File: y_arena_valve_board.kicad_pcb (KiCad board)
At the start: 2 copper layers, 0 parts

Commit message: Initial pcb import
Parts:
- added D1: diode_low_rev_current, y_arena_valve_board:SOD-123, F.Cu at (181.2, 52.2)
- added D10: LED_GRN, y_arena_valve_board:LED0805, F.Cu at (245.0, 25.8)
- added D11: diode_low_rev_current, y_arena_valve_board:SOD-123, F.Cu at (209.4, 52.2)
- added D12: LED_GRN, y_arena_valve_board:LED0805, F.Cu at (213.2, 52.9)
- added D13: diode_low_rev_current, y_arena_valve_board:SOD-123, F.Cu at (227.1, 43.6)
- added D14: LED_GRN, y_arena_valve_board:LED0805, F.Cu at (230.9, 44.2)
- added D15: diode_low_rev_current, y_arena_valve_board:SOD-123, F.Cu at (241.1, 34.4)
- added D16: LED_GRN, y_arena_valve_board:LED0805, F.Cu at (245.0, 35.0)
- added D17: diode_low_rev_current, y_arena_valve_board:SOD-123, F.Cu at (223.5, 52.8)
- added D18: LED_GRN, y_arena_valve_board:LED0805, F.Cu at (227.3, 53.5)
- added D2: LED_GRN, y_arena_valve_board:LED0805, F.Cu at (185.1, 52.9)
- added D3: diode_low_rev_current, y_arena_valve_board:SOD-123, F.Cu at (227.1, 25.1)
- added D4: LED_GRN, y_arena_valve_board:LED0805, F.Cu at (230.9, 25.8)
- added D5: diode_low_rev_current, y_arena_valve_board:SOD-123, F.Cu at (195.3, 52.2)
- added D6: LED_GRN, y_arena_valve_board:LED0805, F.Cu at (199.1, 52.9)
- added D7: diode_low_rev_current, y_arena_valve_board:SOD-123, F.Cu at (227.1, 34.4)
- added D8: LED_GRN, y_arena_valve_board:LED0805, F.Cu at (230.9, 35.0)
- added D9: diode_low_rev_current, y_arena_valve_board:SOD-123, F.Cu at (241.1, 25.1)
- added FID1: FIDUCIAL, y_arena_valve_board:FIDUCIAL, F.Cu at (219.3, 24.9)
- added FID2: FIDUCIAL, y_arena_valve_board:FIDUCIAL, F.Cu at (188.9, 43.5)
- added FID3: FIDUCIAL, y_arena_valve_board:FIDUCIAL, F.Cu at (186.3, 43.5)
- added FID4: FIDUCIAL, y_arena_valve_board:FIDUCIAL, F.Cu at (205.2, 37.2)
- added MH1: MOUNTING_HOLE_4-40, y_arena_valve_board:MOUNTING_HOLE_4-40, F.Cu at (92.1, 101.0)
- added MH2: MOUNTING_HOLE_4-40, y_arena_valve_board:MOUNTING_HOLE_4-40, F.Cu at (120.0, 72.4)
- added MH3: MOUNTING_HOLE_4-40, y_arena_valve_board:MOUNTING_HOLE_4-40, F.Cu at (64.1, 72.4)
- added P1: HEADER_02X12_SMD, y_arena_valve_board:HEADER_02x12_SMD, F.Cu at (213.4, 62.2)
- added R1: 499, y_arena_valve_board:SM0805, F.Cu at (187.7, 52.8)
- added R2: 499, y_arena_valve_board:SM0805, F.Cu at (233.6, 25.7)
- added R3: 499, y_arena_valve_board:SM0805, F.Cu at (201.8, 52.8)
- added R4: 499, y_arena_valve_board:SM0805, F.Cu at (233.6, 35.0)
- added R5: 499, y_arena_valve_board:SM0805, F.Cu at (247.6, 25.7)
- added R6: 499, y_arena_valve_board:SM0805, F.Cu at (215.9, 52.8)
- added R7: 499, y_arena_valve_board:SM0805, F.Cu at (233.6, 44.2)
- added R8: 499, y_arena_valve_board:SM0805, F.Cu at (247.6, 35.0)
- added R9: 499, y_arena_valve_board:SM0805, F.Cu at (230.0, 53.4)
- added S1: LEECO_LHDB, y_arena_valve_board:LEECO_LHDB, B.Cu at (129.5, 33.0)
- added S2: LEECO_LHDB, y_arena_valve_board:LEECO_LHDB, B.Cu at (80.6, 22.2)
- added S3: LEECO_LHDB, y_arena_valve_board:LEECO_LHDB, B.Cu at (80.6, 34.9)
- added S4: LEECO_LHDB, y_arena_valve_board:LEECO_LHDB, B.Cu at (79.4, 53.3)
- added S5: LEECO_LHDB, y_arena_valve_board:LEECO_LHDB, B.Cu at (110.5, 23.5)
- added S6: LEECO_LHDB, y_arena_valve_board:LEECO_LHDB, B.Cu at (101.6, 35.6)
- added S7: LEECO_LHDB, y_arena_valve_board:LEECO_LHDB, B.Cu at (135.9, 54.0)
- added S8: LEECO_LHDB, y_arena_valve_board:LEECO_LHDB, B.Cu at (113.0, 47.0)
- added S9: LEECO_LHDB, y_arena_valve_board:LEECO_LHDB, B.Cu at (160.0, 73.7)
- added SW1: SPST_SLIDE_AS, y_arena_valve_board:SPST_SLIDE_AS, F.Cu at (181.8, 41.7)
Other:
- board outline added: 76.2 x 41.3 mm

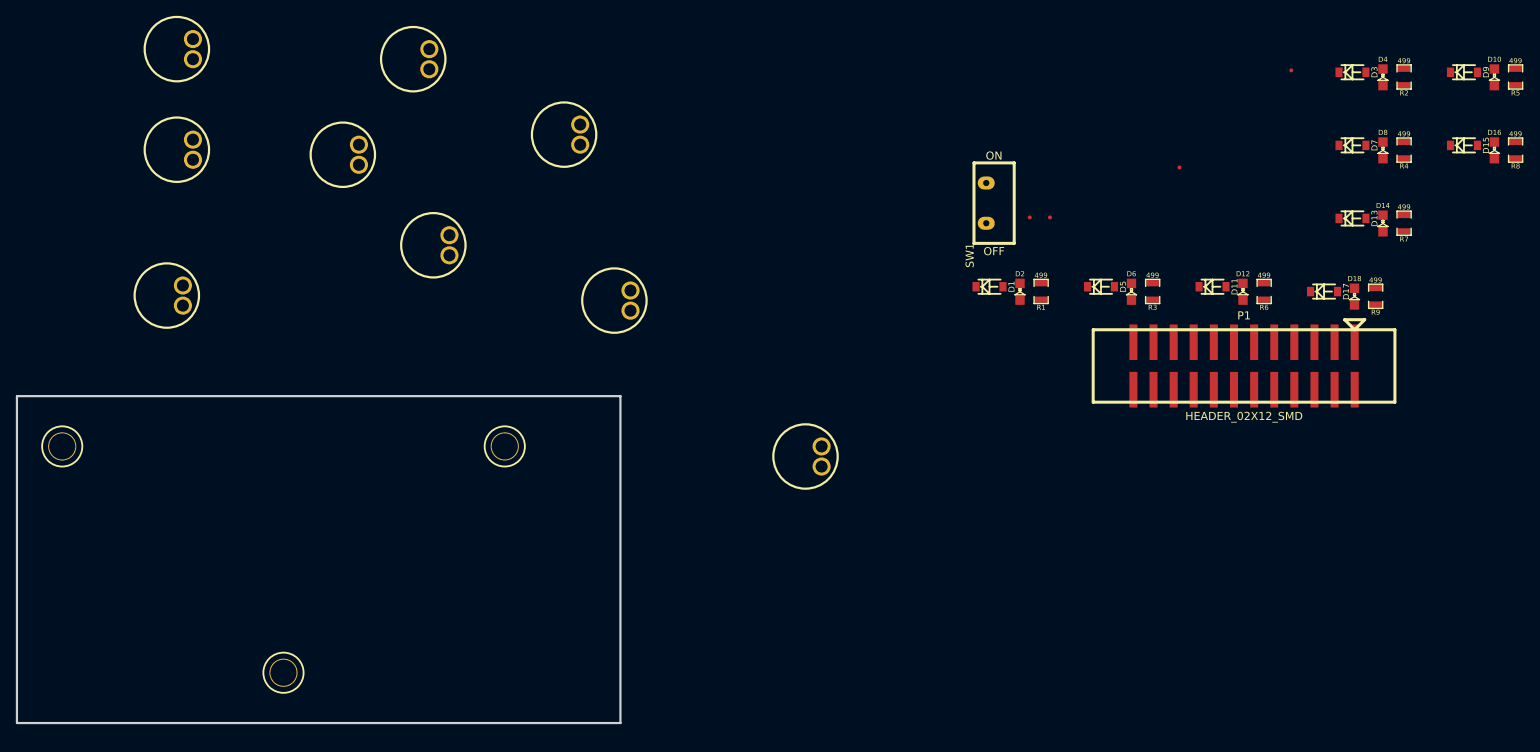
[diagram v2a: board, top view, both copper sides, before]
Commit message: Add footprints to test
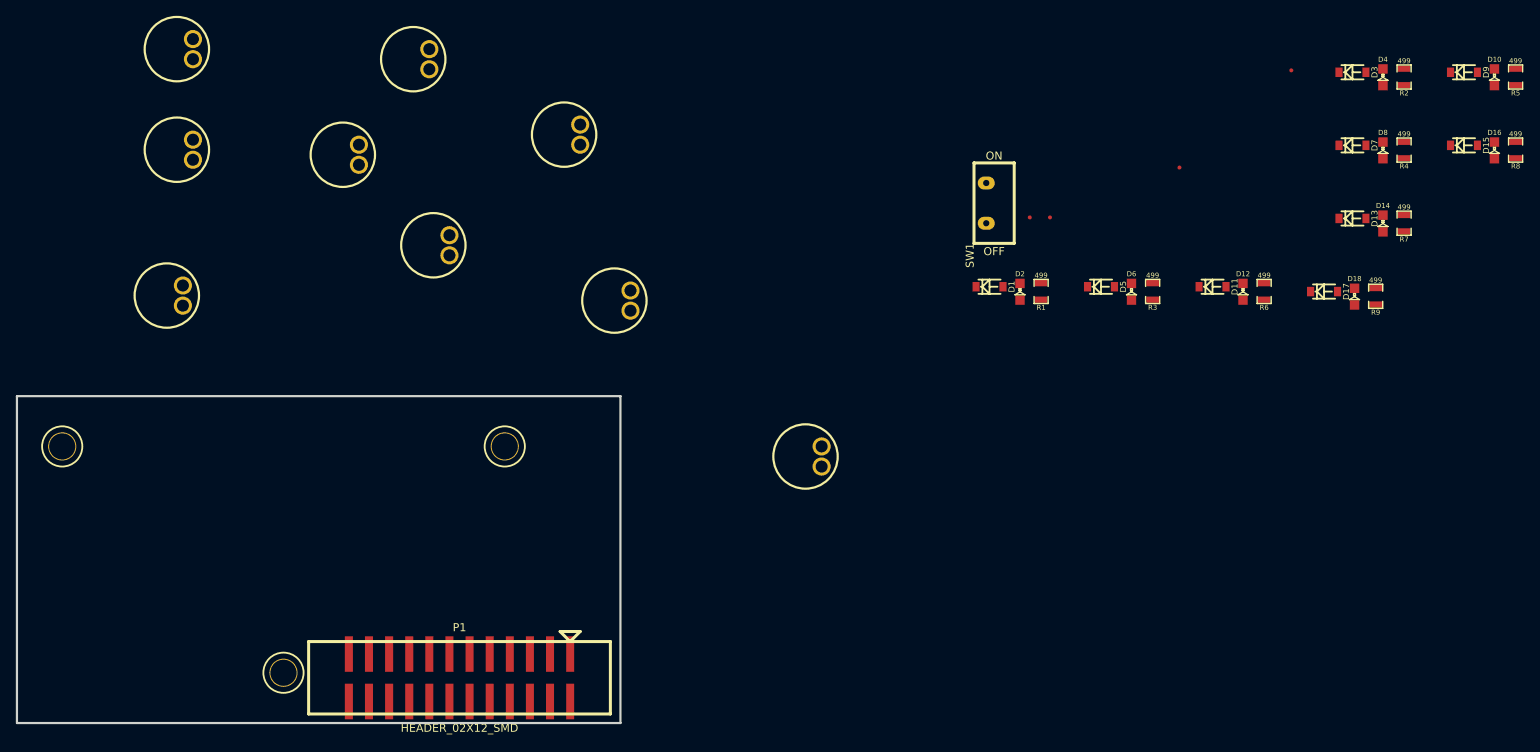
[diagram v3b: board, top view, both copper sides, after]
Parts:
- moved P1 106.6 mm to (114.3, 101.6)
